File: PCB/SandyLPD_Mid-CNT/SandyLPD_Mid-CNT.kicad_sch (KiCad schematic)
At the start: 26 parts

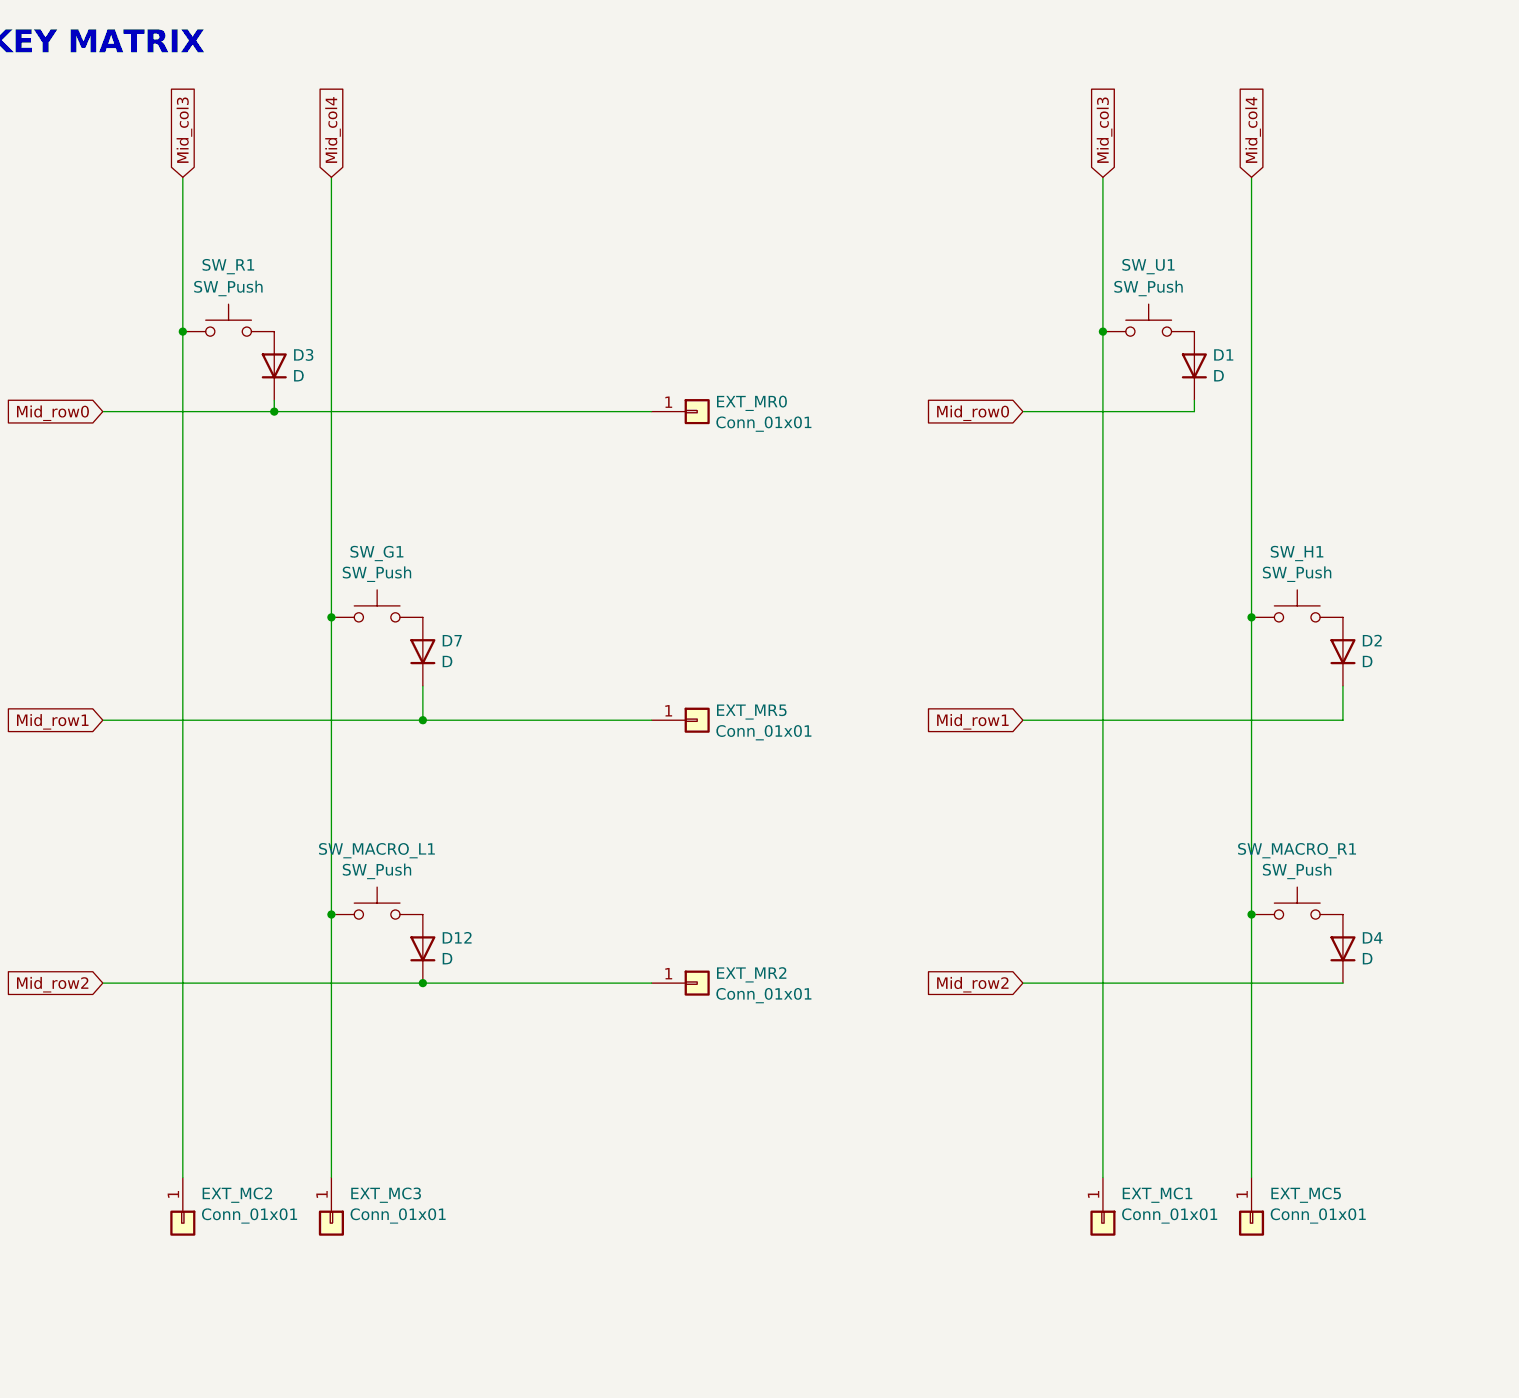
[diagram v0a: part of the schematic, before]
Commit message: Base→MId中央のネジ位置を1箇所変更
Mid中央をリバーシブルにすると、ソケットのパッドと干渉が出たため。
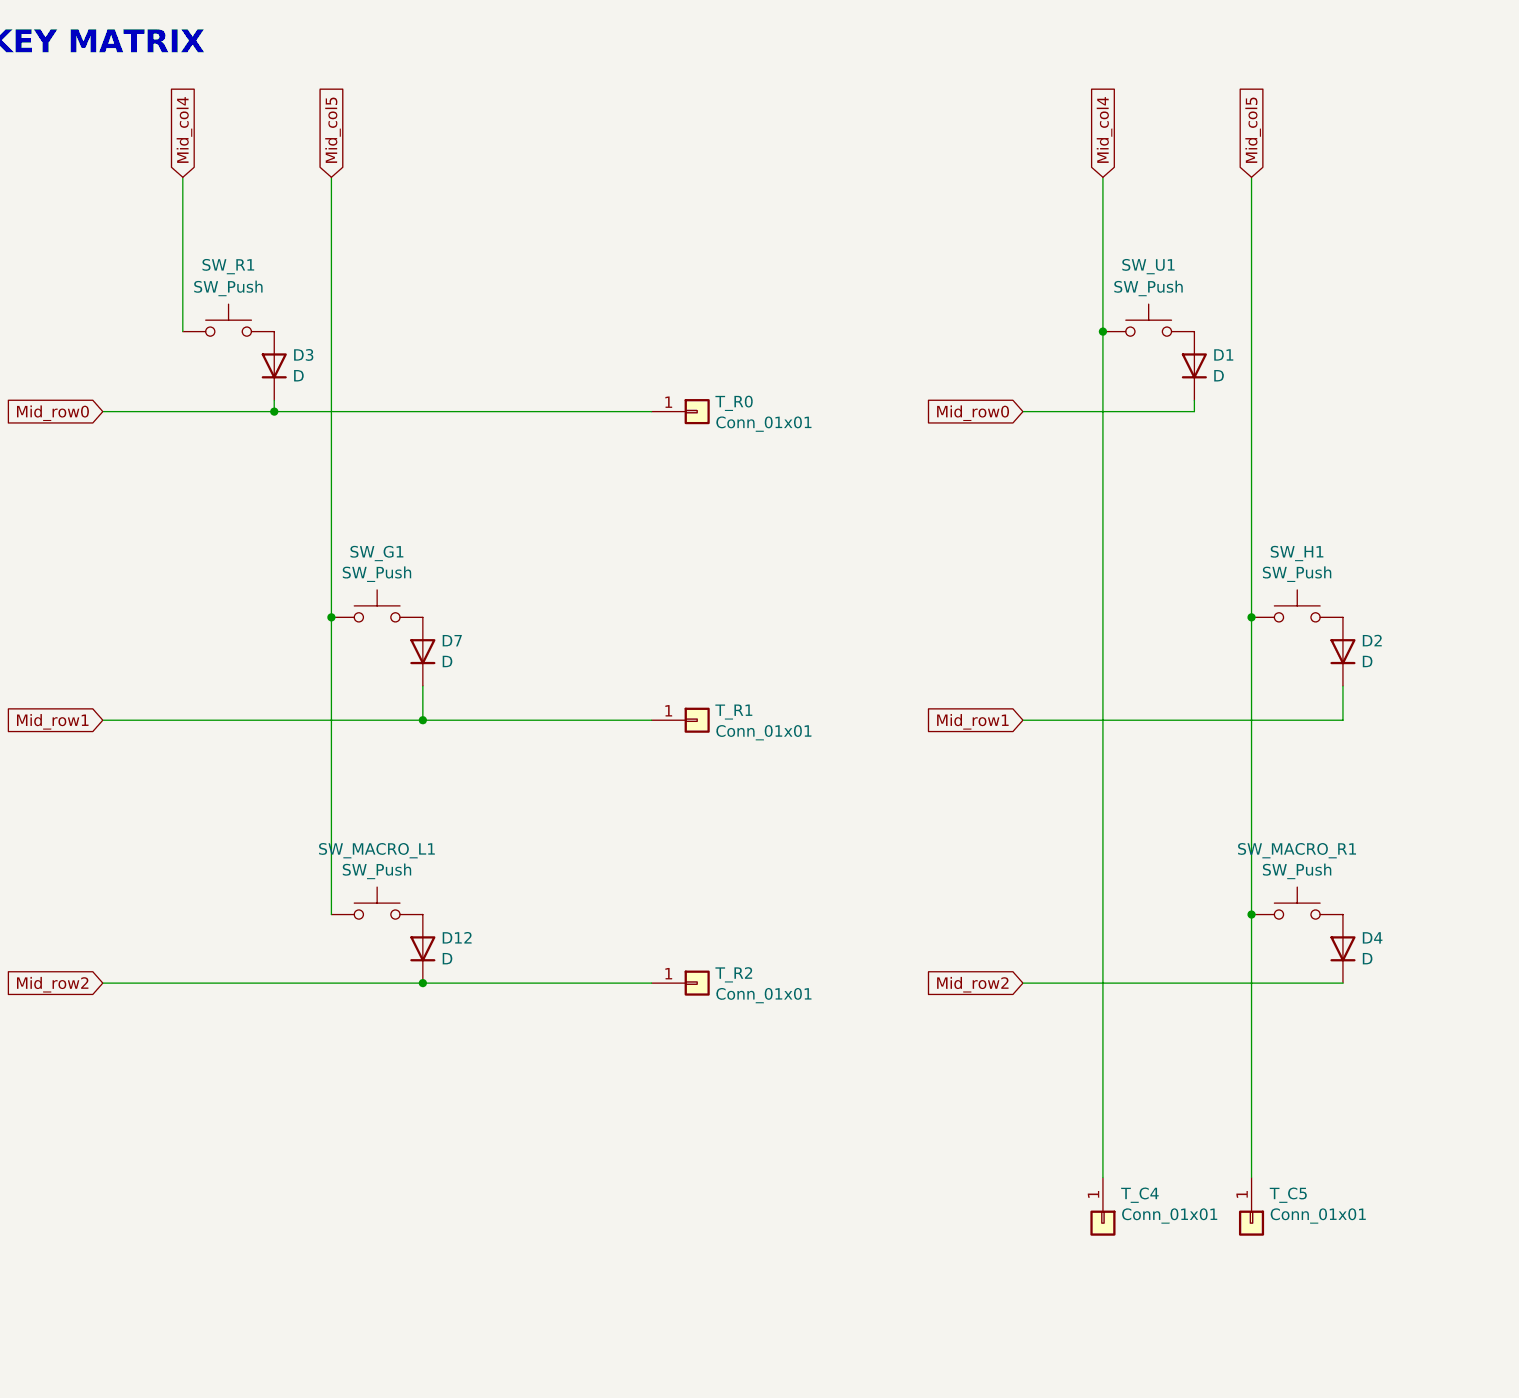
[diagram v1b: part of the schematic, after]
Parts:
- removed EXT_MC2, EXT_MC3: Conn_01x01, locallib:TestPoint_THTPad_D2.0mm_Drill1.0mm, symbol Connector_Generic:Conn_01x01
- SW_H1, SW_U1: footprint locallib:Kailh_socket_ChocV2_small_#2pad -> locallib:Kailh_socket_ChocV2
- SW_MACRO_L1: footprint locallib:Kailh_socket_ChocV2_narrow_#2pad -> locallib:Kailh_socket_ChocV2_small_#2pad
- SW_MACRO_R1: footprint locallib:Kailh_socket_ChocV2_narrow_#2pad -> locallib:Kailh_socket_ChocV2
- renumbered EXT_MC1 to T_C4, EXT_MC5 to T_C5, EXT_MR0 to T_R0, EXT_MR5 to T_R1, EXT_MR2 to T_R2
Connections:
- net Mid_col3 is gone; now on net Mid_col4: SW_R1.1, SW_U1.1, T_C4.1 (Pin_1)
- net Mid_col4: no longer SW_G1.1, SW_H1.1, SW_MACRO_L1.1, SW_MACRO_R1.1, T_C5.1 (Pin_1)
- net Mid_col5: now also SW_G1.1, SW_H1.1, SW_MACRO_L1.1, SW_MACRO_R1.1, T_C5.1 (Pin_1)
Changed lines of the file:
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@@
-	)
-	(junction
-		(at 34.925 47.625)
-		(diameter 0)
-		(color 0 0 0 0)
 	)
 	(junction
@@
 	)
 	(junction
-		(at 51.435 112.395)
-		(diameter 0)
-		(color 0 0 0 0)
-	)
-	(junction
 		(at 45.085 56.515)
 		(diameter 0)
@@
 	(wire
 		(pts
-			(xy 51.435 112.395) (xy 51.435 141.605)
+			(xy 45.085 55.245) (xy 45.085 56.515)
 		)
 		(stroke
@@
 	(wire
 		(pts
-			(xy 45.085 55.245) (xy 45.085 56.515)
+			(xy 128.27 90.805) (xy 163.83 90.805)
 		)
 		(stroke
@@
 	(wire
 		(pts
-			(xy 128.27 90.805) (xy 163.83 90.805)
+			(xy 163.83 86.995) (xy 163.83 90.805)
 		)
 		(stroke
@@
 	(wire
 		(pts
-			(xy 163.83 86.995) (xy 163.83 90.805)
+			(xy 61.595 86.995) (xy 61.595 90.805)
 		)
 		(stroke
@@
 	(wire
 		(pts
-			(xy 61.595 86.995) (xy 61.595 90.805)
+			(xy 153.67 79.375) (xy 153.67 112.395)
 		)
 		(stroke
@@
 	(wire
 		(pts
-			(xy 153.67 79.375) (xy 153.67 112.395)
+			(xy 51.435 30.48) (xy 51.435 79.375)
 		)
 		(stroke
@@
 	(wire
 		(pts
-			(xy 51.435 30.48) (xy 51.435 79.375)
-		)
-		(stroke
-			(width 0)
-			(type default)
-		)
-	)
-	(wire
-		(pts
 			(xy 147.32 55.245) (xy 147.32 56.515)
-		)
-		(stroke
-			(width 0)
-			(type default)
-		)
-	)
-	(wire
-		(pts
-			(xy 34.925 47.625) (xy 34.925 141.605)
 		)
 		(stroke
@@
 	(global_label "Mid_col4"
 		(shape input)
-		(at 51.435 30.48 90)
+		(at 34.925 30.48 90)
 		(fields_autoplaced yes)
 		(effects
@@
 		)
 		(property "Intersheetrefs" "${INTERSHEET_REFS}"
-			(at -118.745 2.54 0)
+			(at -135.255 2.54 0)
 			(effects
 				(font
@@
 		)
 		(property "シート間のリファレンス" "${INTERSHEET_REFS}"
-			(at 51.5144 19.8706 90)
+			(at 35.0044 19.8706 90)
 			(effects
 				(font
@@
 		)
 	)
-	(global_label "Mid_col3"
-		(shape input)
-		(at 34.925 30.48 90)
-		(fields_autoplaced yes)
-		(effects
-			(font
-				(size 1.27 1.27)
-			)
-			(justify left)
-		)
-		(property "Intersheetrefs" "${INTERSHEET_REFS}"
-			(at -102.235 2.54 0)
-			(effects
-				(font
-					(size 1.27 1.27)
-				)
-				(hide yes)
-			)
-		)
-		(property "シート間のリファレンス" "${INTERSHEET_REFS}"
-			(at 35.0044 19.8706 90)
-			(effects
-				(font
-					(size 1.27 1.27)
-				)
-				(justify left)
-				(hide yes)
-			)
-		)
-	)
 	(global_label "Mid_row1"
 		(shape input)
@@
 		)
 	)
-	(global_label "Mid_col3"
+	(global_label "Mid_col4"
 		(shape input)
 		(at 137.16 30.48 90)
@@
 		)
 	)
-	(global_label "Mid_col4"
+	(global_label "Mid_col5"
 		(shape input)
 		(at 153.67 30.48 90)
@@
 		)
 		(property "Intersheetrefs" "${INTERSHEET_REFS}"
-			(at -16.51 2.54 0)
-			(effects
-				(font
-					(size 1.27 1.27)
-				)
+			(at 153.67 19.8639 90)
+			(effects
+				(font
+					(size 1.27 1.27)
+				)
+				(justify left)
 				(hide yes)
 			)
 		)
 		(property "シート間のリファレンス" "${INTERSHEET_REFS}"
-			(at 153.7494 19.8706 90)
+			(at 155.5052 30.48 90)
 			(effects
 				(font
@@
 		)
 	)
-	(symbol
-		(lib_id "Connector_Generic:Conn_01x01")
-		(at 51.435 146.685 270)
-		(unit 1)
-		(exclude_from_sim no)
-		(in_bom yes)
-		(on_board yes)
-		(dnp no)
-		(property "Reference" "EXT_MC3"
-			(at 53.467 143.4338 90)
-			(effects
-				(font
-					(size 1.27 1.27)
-				)
-				(justify left)
-			)
-		)
-		(property "Value" "Conn_01x01"
-			(at 53.467 145.7452 90)
-			(effects
-				(font
-					(size 1.27 1.27)
-				)
-				(justify left)
-			)
-		)
-		(property "Footprint" "locallib:TestPoint_THTPad_D2.0mm_Drill1.0mm"
-			(at 51.435 146.685 0)
-			(effects
-				(font
-					(size 1.27 1.27)
-				)
-				(hide yes)
-			)
-		)
-		(property "Datasheet" "~"
-			(at 51.435 146.685 0)
-			(effects
-				(font
-					(size 1.27 1.27)
-				)
-				(hide yes)
-			)
-		)
-		(property "Description" ""
-			(at 51.435 146.685 0)
-			(effects
-				(font
-					(size 1.27 1.27)
-				)
-				(hide yes)
-			)
-		)
-		(pin "1"
-		)
-		(instances
-			(project "Sandy_Middle"
-				(path "/a99ab643-cdc7-4f8c-8088-c1f4faa914d1"
-					(reference "EXT_MC3")
-					(unit 1)
-				)
+	(global_label "Mid_col5"
+		(shape input)
+		(at 51.435 30.48 90)
+		(fields_autoplaced yes)
+		(effects
+			(font
+				(size 1.27 1.27)
+			)
+			(justify left)
+		)
+		(property "Intersheetrefs" "${INTERSHEET_REFS}"
+			(at 51.435 19.8639 90)
+			(effects
+				(font
+					(size 1.27 1.27)
+				)
+				(justify left)
+				(hide yes)
+			)
+		)
+		(property "シート間のリファレンス" "${INTERSHEET_REFS}"
+			(at 53.2702 30.48 90)
+			(effects
+				(font
+					(size 1.27 1.27)
+				)
+				(justify left)
+				(hide yes)
 			)
 		)
@@
 		(on_board yes)
 		(dnp no)
-		(property "Reference" "EXT_MR0"
+		(property "Reference" "T_R0"
 			(at 94.107 55.4482 0)
 			(effects
@@
 			(project "Sandy_Middle"
 				(path "/a99ab643-cdc7-4f8c-8088-c1f4faa914d1"
-					(reference "EXT_MR0")
+					(reference "T_R0")
 					(unit 1)
 				)
@@
 			)
 		)
-		(property "Footprint" "locallib:Kailh_socket_ChocV2_small_#2pad"
+		(property "Footprint" "locallib:Kailh_socket_ChocV2"
 			(at 158.75 74.295 0)
 			(effects
@@
 		(on_board yes)
 		(dnp no)
-		(property "Reference" "EXT_MC1"
+		(property "Reference" "T_C4"
 			(at 139.192 143.4338 90)
 			(effects
@@
 			(project "SandyLPD_Mid-CNT"
 				(path "/a99ab643-cdc7-4f8c-8088-c1f4faa914d1"
-					(reference "EXT_MC1")
+					(reference "T_C4")
 					(unit 1)
 				)
@@
 		(on_board yes)
 		(dnp no)
-		(property "Reference" "EXT_MR2"
+		(property "Reference" "T_R2"
 			(at 94.107 118.9482 0)
 			(effects
@@
 			(project "Sandy_Middle"
 				(path "/a99ab643-cdc7-4f8c-8088-c1f4faa914d1"
-					(reference "EXT_MR2")
+					(reference "T_R2")
 					(unit 1)
 				)
@@
 		(on_board yes)
 		(dnp no)
-		(property "Reference" "EXT_MR5"
+		(property "Reference" "T_R1"
 			(at 94.107 89.7382 0)
 			(effects
@@
 			(project "Sandy_Middle"
 				(path "/a99ab643-cdc7-4f8c-8088-c1f4faa914d1"
-					(reference "EXT_MR5")
+					(reference "T_R1")
 					(unit 1)
 				)
@@
 			)
 		)
-		(property "Footprint" "locallib:Kailh_socket_ChocV2_narrow_#2pad"
+		(property "Footprint" "locallib:Kailh_socket_ChocV2"
 			(at 158.75 107.315 0)
 			(effects
@@
 		(on_board yes)
 		(dnp no)
-		(property "Reference" "EXT_MC5"
+		(property "Reference" "T_C5"
 			(at 155.702 143.4338 90)
 			(effects
@@
 			(project "SandyLPD_Mid-CNT"
 				(path "/a99ab643-cdc7-4f8c-8088-c1f4faa914d1"
-					(reference "EXT_MC5")
+					(reference "T_C5")
 					(unit 1)
 				)
@@
 			)
 		)
-		(property "Footprint" "locallib:Kailh_socket_ChocV2_small_#2pad"
+		(property "Footprint" "locallib:Kailh_socket_ChocV2"
 			(at 142.24 42.545 0)
 			(effects
@@
 				(path "/a99ab643-cdc7-4f8c-8088-c1f4faa914d1"
 					(reference "SW_U1")
-					(unit 1)
-				)
-			)
-		)
-	)
-	(symbol
-		(lib_id "Connector_Generic:Conn_01x01")
-		(at 34.925 146.685 270)
-		(unit 1)
-		(exclude_from_sim no)
-		(in_bom yes)
-		(on_board yes)
-		(dnp no)
-		(property "Reference" "EXT_MC2"
-			(at 36.957 143.4338 90)
-			(effects
-				(font
-					(size 1.27 1.27)
-				)
-				(justify left)
-			)
-		)
-		(property "Value" "Conn_01x01"
-			(at 36.957 145.7452 90)
-			(effects
-				(font
-					(size 1.27 1.27)
-				)
-				(justify left)
-			)
-		)
-		(property "Footprint" "locallib:TestPoint_THTPad_D2.0mm_Drill1.0mm"
-			(at 34.925 146.685 0)
-			(effects
-				(font
-					(size 1.27 1.27)
-				)
-				(hide yes)
-			)
-		)
-		(property "Datasheet" "~"
-			(at 34.925 146.685 0)
-			(effects
-				(font
-					(size 1.27 1.27)
-				)
-				(hide yes)
-			)
-		)
-		(property "Description" ""
-			(at 34.925 146.685 0)
-			(effects
-				(font
-					(size 1.27 1.27)
-				)
-				(hide yes)
-			)
-		)
-		(pin "1"
-		)
-		(instances
-			(project "Sandy_Middle"
-				(path "/a99ab643-cdc7-4f8c-8088-c1f4faa914d1"
-					(reference "EXT_MC2")
 					(unit 1)
 				)
@@
 			)
 		)
-		(property "Footprint" "locallib:Kailh_socket_ChocV2_narrow_#2pad"
+		(property "Footprint" "locallib:Kailh_socket_ChocV2_small_#2pad"
 			(at 56.515 107.315 0)
 			(effects
